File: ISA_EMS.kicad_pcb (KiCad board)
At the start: 2 copper layers, 176.5 x 102.9 mm, 91 parts, among them J1 ISA BUS, J10 Parallel Port, J11 Serial 4 IDC, J12 Serial 3 IDC, J13 UART4_SEL, J14 ROM Config, J2 ADDR_IRQ, J3 UART1_SEL, J4 UART2_SEL, J5 ADDR, J6 Serial 2 IDC, J7 Serial 1 DB9, J8 UART3_SEL, J9 Parport IRQ Select, U1 74LS138, U11 74LS30, U12 74LS86, U13 74LS02, U14 74LS155, U15 74LS245, U16 74LS174, U17 74LS374, U18 74LS05, U19 74LS125, U2 74LS138, U20 74LS240, U21 74LS244, U23 16C554, U24 74LS32, U25 GD75232N, U26 GD75232N, U27 SST39SF040, U28 74HCT688, U5 GD75232N, U6 GD75232N, X1 1.8432Mhz

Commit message: Update schematic, draw board
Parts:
- removed C27, C28, C29, C30, C31, C32, C33, C34, C35: 2.2nF, Capacitor_THT:C_Disc_D5.0mm_W2.5mm_P5.00mm
- removed D2: LED Channel B, LED_THT:LED_D3.0mm-3
- removed D3: LED Channel C, LED_THT:LED_D3.0mm-3
- removed D4: LED Channel D, LED_THT:LED_D3.0mm-3
- removed J10: Parallel Port, Connector_PinHeader_2.54mm:PinHeader_2x13_P2.54mm_Vertical
- removed J11: Serial 4 IDC, Connector_PinHeader_2.54mm:PinHeader_2x05_P2.54mm_Vertical
- removed J12: Serial 3 IDC, Connector_PinHeader_2.54mm:PinHeader_2x05_P2.54mm_Vertical
- removed J13: UART4_SEL, Connector_PinHeader_2.54mm:PinHeader_1x04_P2.54mm_Vertical
- removed the J3 at (227.4, 159.1)
- removed J4: UART2_SEL, Connector_PinHeader_2.54mm:PinHeader_1x08_P2.54mm_Vertical
- removed J5: ADDR, Connector_PinHeader_2.54mm:PinHeader_1x04_P2.54mm_Vertical
- removed J6: Serial 2 IDC, Connector_PinHeader_2.54mm:PinHeader_2x05_P2.54mm_Vertical
- removed J7: Serial 1 DB9, Connector_Dsub:DSUB-9_Male_Horizontal_P2.77x2.84mm_EdgePinOffset7.70mm_Housed_MountingHolesOffset9.12mm
- removed J8: UART3_SEL, Connector_PinHeader_2.54mm:PinHeader_1x04_P2.54mm_Vertical
- removed J9: Parport IRQ Select, Connector_PinHeader_2.54mm:PinHeader_2x04_P2.54mm_Vertical
- removed JP1: Address selection, Connector_PinHeader_2.54mm:PinHeader_1x02_P2.54mm_Vertical
- removed JP2: Parport type, Connector_PinHeader_2.54mm:PinHeader_1x03_P2.54mm_Vertical
- removed JP3: Interrupt Mode, Connector_PinHeader_2.54mm:PinHeader_1x02_P2.54mm_Vertical
- removed R10, R4, R5, R6, R7, R8, R9: 1k, Resistor_THT:R_Axial_DIN0207_L6.3mm_D2.5mm_P10.16mm_Horizontal
- removed the RN1 at (144.8, 124.5)
- removed the U1 at (271.8, 190.5)
- removed the U2 at (271.8, 179.1)
- removed U23: 16C554, Package_LCC:PLCC-68_THT-Socket
- removed U24: 74LS32, Package_DIP:DIP-14_W7.62mm_LongPads
- removed U25, U26: GD75232N, Package_DIP:DIP-20_W7.62mm_LongPads
- removed X1: 1.8432Mhz, ISA_DualUART:Oscillator_DIP-14-8
- added C21: 100nF, Capacitor_THT:C_Disc_D6.0mm_W2.5mm_P5.00mm, F.Cu at (254.0, 104.1)
- added RN3: 10k, Resistor_THT:R_Array_SIP9, F.Cu at (224.8, 177.8)
- added U10: 74HCT32, Package_DIP:DIP-14_W7.62mm_LongPads, F.Cu at (223.5, 156.2)
- added U3: AS6C4008-55PCN, Package_DIP:DIP-32_W15.24mm, F.Cu at (162.6, 108.0)
- added U4: AS6C4008-55PCN, Package_DIP:DIP-32_W15.24mm, F.Cu at (142.2, 108.0)
- added U7: 74HCT688, Package_DIP:DIP-20_W7.62mm_LongPads, F.Cu at (177.8, 190.5)
- added U8: 74HCT688, Package_DIP:DIP-20_W7.62mm_LongPads, F.Cu at (146.1, 190.5)
- added U9: 74HCT139, Package_DIP:DIP-16_W7.62mm_LongPads, F.Cu at (208.3, 153.7)
- D1: value LED Channel A -> EMS in use; footprint LED_THT:LED_D3.0mm-3 -> LED_THT:LED_D3.0mm_Clear
- J2: value ADDR_IRQ -> EMS Address; footprint Connector_PinHeader_2.54mm:PinHeader_1x08_P2.54mm_Vertical -> Connector_PinHeader_2.54mm:PinHeader_2x04_P2.54mm_Vertical
- RN2: value 4.7k -> 10k
- U11: value 74LS30 -> 74HCT04
- U12: value 74LS86 -> 74ACT245; footprint Package_DIP:DIP-14_W7.62mm_LongPads -> Package_DIP:DIP-20_W7.62mm_LongPads
- U13: value 74LS02 -> AS6C4008-55PCN; footprint Package_DIP:DIP-14_W7.62mm_LongPads -> Package_DIP:DIP-32_W15.24mm
- U14: value 74LS155 -> AS6C4008-55PCN; footprint Package_DIP:DIP-16_W7.62mm_LongPads -> Package_DIP:DIP-32_W15.24mm
- U15: value 74LS245 -> AS6C4008-55PCN; footprint Package_DIP:DIP-20_W7.62mm_LongPads -> Package_DIP:DIP-32_W15.24mm
- U16: value 74LS174 -> AS6C4008-55PCN; footprint Package_DIP:DIP-16_W7.62mm_LongPads -> Package_DIP:DIP-32_W15.24mm
- U17: value 74LS374 -> 74HCT138; footprint Package_DIP:DIP-20_W7.62mm_LongPads -> Package_DIP:DIP-16_W7.62mm_LongPads
- U18: value 74LS05 -> 74LS573; footprint Package_DIP:DIP-14_W7.62mm_LongPads -> Package_DIP:DIP-20_W7.62mm_LongPads
- U19: value 74LS125 -> 74LS573; footprint Package_DIP:DIP-14_W7.62mm_LongPads -> Package_DIP:DIP-20_W7.62mm_LongPads
- U20: value 74LS240 -> 74LS573
- U21: value 74LS244 -> 74LS573
- U5, U6: value GD75232N -> AS6C4008-55PCN; footprint Package_DIP:DIP-20_W7.62mm_LongPads -> Package_DIP:DIP-32_W15.24mm
- moved C17 155.1 mm to (142.2, 184.2)
- moved C38 153.6 mm to (294.6, 104.1), turned to 180 degrees
- moved U5 127.9 mm to (182.9, 108.0), turned to 0 degrees
- moved U16 127.8 mm to (284.5, 108.0), turned to 0 degrees
- moved D1 114.3 mm to (304.8, 105.4), turned to 90 degrees
- moved R3 113.0 mm to (304.8, 121.9), turned to 90 degrees
- moved U6 104.9 mm to (203.2, 108.0), turned to 0 degrees
- moved C11 96.7 mm to (174.0, 184.2)
- moved C40 87.7 mm to (152.4, 104.1), turned to 180 degrees
- moved RN1 85.3 mm to (285.8, 157.5)
- moved J3 85.3 mm to (283.2, 163.8)
- moved C36 85.1 mm to (213.4, 104.1), turned to 180 degrees
- moved U14 82.6 mm to (243.8, 108.0), turned to 0 degrees
- moved U13 82.5 mm to (223.5, 108.0), turned to 0 degrees
- moved C2 74.5 mm to (224.8, 152.4), turned to 0 degrees
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- renumbered J14 to J3, RN3 to RN1, U28 to U1, U27 to U2
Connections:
- J1 pad 14: /~IOR -> (no net)
- J1 pad 2: /RESETDRV -> (no net)
- J1 pad 21: /IRQ7 -> (no net)
- J1 pad 23: /IRQ5 -> (no net)
- J1 pad 24: /IRQ4 -> (no net)
- J1 pad 25: /IRQ3 -> (no net)
- J2 pad 1: /IRQ3 -> GND
- J2 pad 2: /IRQ4 -> /JP1
- J2 pad 3: /IRQ5 -> GND
- J2 pad 4: /IRQ7 -> /JP2
- J2 pad 5: /0x2E8 -> GND
- J2 pad 6: /0x3E8 -> /JP3
- J2 pad 7: /0x2F8 -> GND
- J2 pad 8: /0x3F8 -> /JP4
- R3 pad 1: Net-(D1-Pad1) -> /~RAM-SELECT
- R3 pad 2: /TX_A -> Net-(D1-Pad1)
- RN2 pad 2: /~UART1_CS -> /JP1
- RN2 pad 3: /~UART2_CS -> /JP2
- RN2 pad 4: /~UART3_CS -> /JP3
- RN2 pad 5: /~UART4_CS -> /JP4
- U11 pad 11: /A9 -> GND
- U11 pad 12: /A9 -> (no net)
- U11 pad 13: (no net) -> GND
- U11 pad 2: Net-(U11-Pad2) -> /REG0-LOAD
- U11 pad 3: /A3 -> Net-(U11-Pad3)
- U11 pad 4: /A4 -> /REG1-LOAD
- U11 pad 5: /A5 -> Net-(U11-Pad5)
- U11 pad 6: /A6 -> /REG2-LOAD
- U11 pad 8: Net-(U11-Pad8) -> /REG3-LOAD
- U11 pad 9: (no net) -> Net-(U11-Pad9)
- U12 pad 1: /PARPORT_PE -> /~MEMR
- U12 pad 10: VCC -> GND
- U12 pad 11: /PARPORT_IRQ -> /DB7
- U12 pad 12: VCC -> /DB6
- U12 pad 13: /RN_7 -> /DB5
- U12 pad 14: VCC -> /DB4
- U12 pad 2: VCC -> /D0
- U12 pad 3: Net-(U12-Pad3) -> /D1
- U12 pad 4: /RN_1 -> /D2
- U12 pad 5: /A8 -> /D3
- U12 pad 6: Net-(U11-Pad2) -> /D4
- U12 pad 7: GND -> /D5
- U12 pad 8: /~PARPORT_IRQEN -> /D6
- U12 pad 9: /PARPORT_IRQEN -> /D7
- U13 pad 1: Net-(U13-Pad1) -> /RAM-A18
- U13 pad 10: /PARPORT_R -> /A2
- U13 pad 11: /RESETDRV -> /A1
- U13 pad 12: /RESETDRV -> /A0
- U13 pad 13: /~PARPORT_RESET -> /DB0
- U13 pad 14: VCC -> /DB1
- U13 pad 2: /PARPORT_SLCT -> /RAM-A16
- U13 pad 3: /PARPORT_SLCT -> /RAM-A14
- U13 pad 4: Net-(U11-Pad1) -> /A12
- U13 pad 6: /AEN -> /A6
- U13 pad 7: GND -> /A5
- U13 pad 8: Net-(U11-Pad8) -> /A4
- U13 pad 9: /~IOR -> /A3
- U14 pad 1: /PARPORT_R -> /RAM-A18
- U14 pad 10: (no net) -> /A2
- U14 pad 11: /PARPORT_WPC -> /A1
- U14 pad 12: (no net) -> /A0
- U14 pad 13: /A0 -> /DB0
- U14 pad 14: /~IOW -> /DB1
- U14 pad 15: Net-(U11-Pad8) -> /DB2
- U14 pad 16: VCC -> GND
- U14 pad 2: GND -> /RAM-A16
- U14 pad 3: /A1 -> /RAM-A14
- U14 pad 4: (no net) -> /A12
- U14 pad 5: /PARPORT_RPC -> /A7
- U14 pad 6: /PARPORT_RPB -> /A6
- U14 pad 7: /PARPORT_RPA -> /A5
- U14 pad 8: GND -> /A4
- U14 pad 9: /PARPORT_WPA -> /A3
- U15 pad 1: /PARPORT_R -> /RAM-A18
- U15 pad 10: GND -> /A2
- U15 pad 11: /D7 -> /A1
- U15 pad 12: /D6 -> /A0
- U15 pad 13: /D5 -> /DB0
- U15 pad 14: /D4 -> /DB1
- U15 pad 15: /D3 -> /DB2
- U15 pad 16: /D2 -> GND
- U15 pad 17: /D1 -> /DB3
- U15 pad 18: /D0 -> /DB4
- U15 pad 19: GND -> /DB5
- U15 pad 2: /PARPORT_BD0 -> /RAM-A16
- U15 pad 20: VCC -> /DB6
- U15 pad 3: /PARPORT_BD1 -> /RAM-A14
- U15 pad 4: /PARPORT_BD2 -> /A12
- U15 pad 5: /PARPORT_BD3 -> /A7
- U15 pad 6: /PARPORT_BD4 -> /A6
- U15 pad 7: /PARPORT_BD5 -> /A5
- U15 pad 8: /PARPORT_BD6 -> /A4
- U15 pad 9: /PARPORT_BD7 -> /A3
- U16 pad 1: /~PARPORT_RESET -> /RAM-A18
- U16 pad 10: Net-(U16-Pad10) -> /A2
- U16 pad 11: /PARPORT_BD3 -> /A1
- U16 pad 12: /PARPORT_IRQEN -> /A0
- U16 pad 13: /PARPORT_BD4 -> /DB0
- U16 pad 14: /PARPORT_BD5 -> /DB1
- U16 pad 15: /PARPORT_DIR -> /DB2
- U16 pad 16: VCC -> GND
- U16 pad 2: Net-(U16-Pad2) -> /RAM-A16
- U16 pad 3: /PARPORT_BD0 -> /RAM-A14
- U16 pad 4: /PARPORT_BD1 -> /A12
- U16 pad 5: Net-(U16-Pad5) -> /A7
- U16 pad 6: /PARPORT_BD2 -> /A6
- U16 pad 7: Net-(U16-Pad7) -> /A5
- U16 pad 8: GND -> /A4
- U16 pad 9: /PARPORT_WPC -> /A3
- U17 pad 1: Net-(JP2-Pad2) -> /RAM-A19
- U17 pad 10: GND -> /~RAM-CS5
- U17 pad 11: /PARPORT_WPA -> /~RAM-CS4
- U17 pad 12: /PARPORT_DATA3 -> /~RAM-CS3
- U17 pad 13: /PARPORT_BD3 -> /~RAM-CS2
- U17 pad 14: /PARPORT_BD2 -> /~RAM-CS1
- U17 pad 15: /PARPORT_DATA2 -> /~RAM-CS0
- U17 pad 16: /PARPORT_DATA1 -> VCC
- U17 pad 2: /PARPORT_DATA4 -> /RAM-A20
- U17 pad 3: /PARPORT_BD4 -> /RAM-A21
- U17 pad 4: /PARPORT_BD5 -> GND
- U17 pad 5: /PARPORT_DATA5 -> /~RAM-SELECT
- U17 pad 6: /PARPORT_DATA6 -> VCC
- U17 pad 7: /PARPORT_BD6 -> /~RAM-CS7
- U17 pad 8: /PARPORT_BD7 -> GND
- U17 pad 9: /PARPORT_DATA7 -> /~RAM-CS6
- U18 pad 1: Net-(U16-Pad2) -> /~REG0-OE
- U18 pad 10: /RN_4 -> GND
- U18 pad 11: /RN_3 -> /REG0-LOAD
- U18 pad 12: /RN_8 -> /RAM-A21
- U18 pad 13: /RN_4 -> /RAM-A20
- U18 pad 14: VCC -> /RAM-A19
- U18 pad 2: /RN_6 -> /D0
- U18 pad 3: Net-(U16-Pad7) -> /D1
- U18 pad 4: /RN_3 -> /D2
- U18 pad 5: Net-(U16-Pad5) -> /D3
- U18 pad 6: /RN_5 -> /D4
- U18 pad 7: GND -> /D5
- U18 pad 8: /RN_2 -> /D6
- U18 pad 9: Net-(U16-Pad10) -> /D7
- U19 pad 1: VCC -> /~REG1-OE
- U19 pad 10: /PARPORT_RPC -> GND
- U19 pad 11: Net-(J9-Pad2) -> /REG1-LOAD
- U19 pad 12: /RN_7 -> /RAM-A21
- U19 pad 13: /~PARPORT_IRQEN -> /RAM-A20
- U19 pad 14: VCC -> /RAM-A19
- U19 pad 2: VCC -> /D0
- U19 pad 3: (no net) -> /D1
- U19 pad 4: /PARPORT_RPB -> /D2
- U19 pad 5: /~PARPORT_ERROR -> /D3
- U19 pad 6: /PARPORT_BD3 -> /D4
- U19 pad 7: GND -> /D5
- U19 pad 8: /PARPORT_BD4 -> /D6
- U19 pad 9: /PARPORT_IRQEN -> /D7
- U20 pad 1: /PARPORT_RPB -> /~REG2-OE
- U20 pad 11: /RN_2 -> /REG2-LOAD
- U20 pad 12: /PARPORT_BD7 -> /RAM-A21
- U20 pad 13: /RN_8 -> /RAM-A20
- U20 pad 14: /PARPORT_BD6 -> /RAM-A19
- U20 pad 15: /RN_5 -> /RAM-A18
- U20 pad 16: /PARPORT_BD5 -> /RAM-A17
- U20 pad 17: /RN_6 -> /RAM-A16
- U20 pad 18: /PARPORT_BD4 -> /RAM-A15
- U20 pad 19: /PARPORT_RPC -> /RAM-A14
- U20 pad 2: Net-(U13-Pad1) -> /D0
- U20 pad 3: /PARPORT_BD0 -> /D1
- U20 pad 4: Net-(U12-Pad3) -> /D2
- U20 pad 5: /PARPORT_BD1 -> /D3
- U20 pad 6: /PARPORT_IRQ -> /D4
- U20 pad 7: /PARPORT_BD2 -> /D5
- U20 pad 8: /PARPORT_BUSY -> /D6
- U20 pad 9: /PARPORT_BD3 -> /D7
- U21 pad 1: /PARPORT_RPA -> /~REG3-OE
- U21 pad 11: /PARPORT_DATA3 -> /REG3-LOAD
- U21 pad 12: /PARPORT_BD7 -> /RAM-A21
- U21 pad 13: /PARPORT_DATA2 -> /RAM-A20
- U21 pad 14: /PARPORT_BD6 -> /RAM-A19
- U21 pad 15: /PARPORT_DATA1 -> /RAM-A18
- U21 pad 16: /PARPORT_BD5 -> /RAM-A17
- U21 pad 17: /PARPORT_DATA0 -> /RAM-A16
- U21 pad 18: /PARPORT_BD4 -> /RAM-A15
- U21 pad 19: /PARPORT_RPA -> /RAM-A14
- U21 pad 2: /PARPORT_DATA4 -> /D0
- U21 pad 3: /PARPORT_BD0 -> /D1
- U21 pad 4: /PARPORT_DATA5 -> /D2
- U21 pad 5: /PARPORT_BD1 -> /D3
- U21 pad 6: /PARPORT_DATA6 -> /D4
- U21 pad 7: /PARPORT_BD2 -> /D5
- U21 pad 8: /PARPORT_DATA7 -> /D6
- U21 pad 9: /PARPORT_BD3 -> /D7
- U5 pad 1: +12V -> /RAM-A18
- U5 pad 10: -12V -> /A2
- U5 pad 11: GND -> /A1
- U5 pad 12: /~RI_A -> /A0
- U5 pad 13: /~DTR_A -> /DB0
- U5 pad 14: /~CTS_A -> /DB1
- U5 pad 15: /TX_A -> /DB2
- U5 pad 16: /~RTS_A -> GND
- U5 pad 17: /RX_A -> /DB3
- U5 pad 18: /~DSR_A -> /DB4
- U5 pad 19: /~DCD_A -> /DB5
- U5 pad 2: /RS232_1_DCD -> /RAM-A16
- U5 pad 20: VCC -> /DB6
- U5 pad 3: /RS232_1_DSR -> /RAM-A14
- U5 pad 4: /RS232_1_RX -> /A12
- U5 pad 5: /RS232_1_RTS -> /A7
- U5 pad 6: /RS232_1_TX -> /A6
- U5 pad 7: /RS232_1_CTS -> /A5
- U5 pad 8: /RS232_1_DTR -> /A4
- U5 pad 9: /RS232_1_RI -> /A3
- U6 pad 1: +12V -> /RAM-A18
- U6 pad 10: -12V -> /A2
- U6 pad 11: GND -> /A1
- U6 pad 12: /~RI_B -> /A0
- U6 pad 13: /~DTR_B -> /DB0
- U6 pad 14: /~CTS_B -> /DB1
- U6 pad 15: /TX_B -> /DB2
- U6 pad 16: /~RTS_B -> GND
- U6 pad 17: /RX_B -> /DB3
- U6 pad 18: /~DSR_B -> /DB4
- U6 pad 19: /~DCD_B -> /DB5
- U6 pad 2: /RS232_2_DCD -> /RAM-A16
- U6 pad 20: VCC -> /DB6
- U6 pad 3: /RS232_2_DSR -> /RAM-A14
- U6 pad 4: /RS232_2_RX -> /A12
- U6 pad 5: /RS232_2_RTS -> /A7
- U6 pad 6: /RS232_2_TX -> /A6
- U6 pad 7: /RS232_2_CTS -> /A5
- U6 pad 8: /RS232_2_DTR -> /A4
- U6 pad 9: /RS232_2_RI -> /A3
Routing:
- net GND: track 995.6 -> 0.00 mm, vias 1 -> 0
- net VCC: track 784.3 -> 0.00 mm, vias 1 -> 0
- net /~IOW: track 221.8 -> 0.00 mm, vias 5 -> 0
- net /A5: track 215.0 -> 0.00 mm, vias 3 -> 0
- net /A3: track 214.5 -> 0.00 mm, vias 3 -> 0
- net +12V: track 212.6 -> 0.00 mm, vias 2 -> 0
- net /A4: track 211.9 -> 0.00 mm, vias 4 -> 0
- net /RESETDRV: track 209.8 -> 0.00 mm, vias 2 -> 0
- net /A6: track 206.4 -> 0.00 mm, vias 2 -> 0
- net /D6: track 204.3 -> 0.00 mm, vias 4 -> 0
- net -12V: track 195.6 -> 0.00 mm, vias 1 -> 0
- net /A1: track 190.6 -> 0.00 mm, vias 5 -> 0
- net /D7: track 189.2 -> 0.00 mm, vias 1 -> 0
- net /A0: track 176.4 -> 0.00 mm, vias 4 -> 0
- net /PARPORT_IRQ: track 175.4 -> 0.00 mm, vias 1 -> 0
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- removed copper zone on B.Cu, net GND
- removed copper zone on F.Cu, net GND
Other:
- board text removed: "1-2 -> Bidirectional 2-3 -> SPP (default)"
- board text removed: "1.8432Mhz"
- board text removed: "10k"
- board text removed: "10k Bussed"
- board text removed: "10uF"
- board text removed: "16C554"
- board text removed: "1k"
- board text removed: "2E8"
- board text removed: "2F8"
- board text removed: "32K"
- board text removed: "3E8"
- board text removed: "3F8"
- board text removed: "4.7k Bussed"
- board text removed: "4.7k bussed"
- board text removed: "64K"
- board text removed: "74HCT688"
- board text removed: "74LS02"
- board text removed: "74LS05"
- board text removed: "74LS125"
- board text removed: "74LS138"
- board text removed: "74LS155"
- board text removed: "74LS174"
- board text removed: "74LS240"
- board text removed: "74LS244"
- board text removed: "74LS245"
- board text removed: "74LS30"
- board text removed: "74LS32"
- board text removed: "74LS374"
- board text removed: "74LS86"
- board text removed: "75232"
- board text removed: "<- 9x 2.2nF ->"
- board text removed: "A15"
- board text removed: "A16"
- board text removed: "A17"
- board text removed: "A18"
- board text removed: "Ch.1"
- board text removed: "Ch.2"
- board text removed: "Ch.3"
- board text removed: "Ch.4"
- board text removed: "ENA"
- board text removed: "INT Mode"
- board text removed: "IRQ3"
- board text removed: "IRQ4"
- board text removed: "IRQ5"
- board text removed: "IRQ7"
- board text removed: "Open -> 0x278 Closed -> 0x378"
- board text removed: "ParPort IRQ"
- board text removed: "Parallel Port"
- board text removed: "ROM EXP"
- board text removed: "SER1"
- board text removed: "SER2"
- board text removed: "SER3"
- board text removed: "SER4"
- board text removed: "SST39SF0x0"
- board text removed: "Serial / Parallel / ROM ISA Board - 1.0 by hkz"
- board text removed: "Serial port 1"
- board text removed: "Serial port 2"
- board text removed: "Serial port 3"
- board text removed: "Serial port 4"

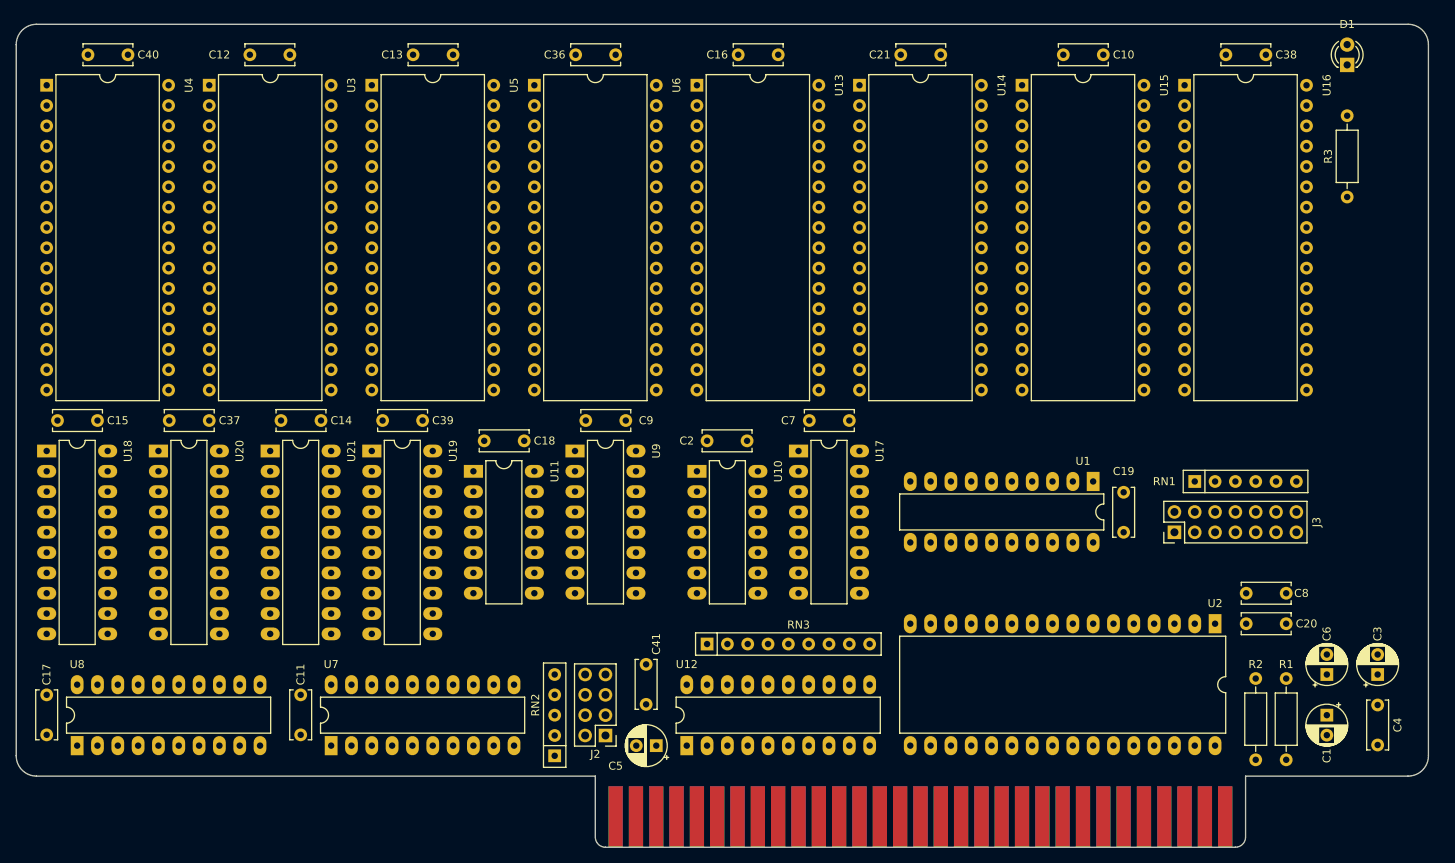
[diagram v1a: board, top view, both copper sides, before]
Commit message: Routed the board
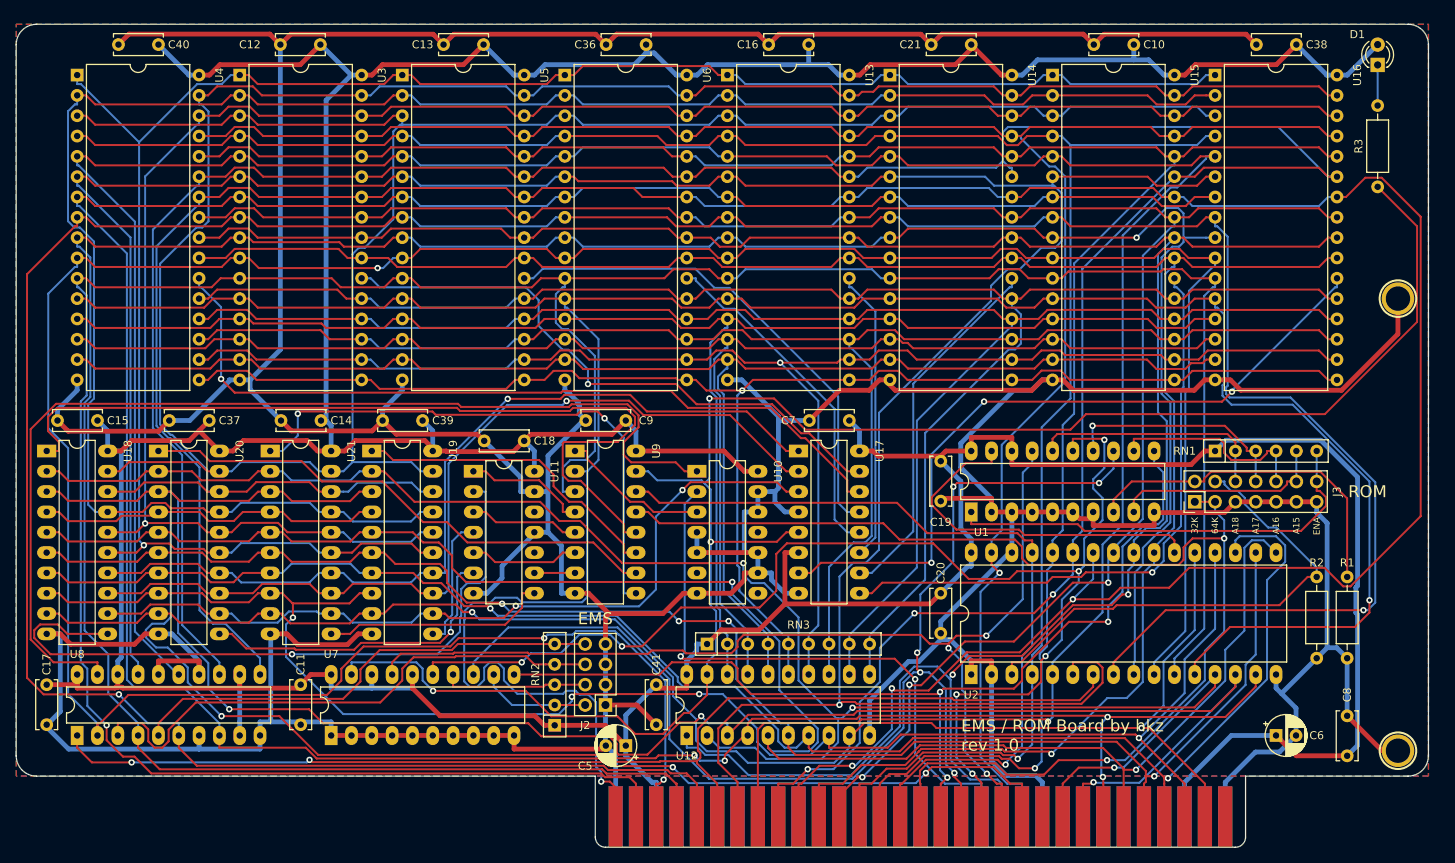
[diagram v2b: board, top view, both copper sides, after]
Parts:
- removed C1, C3: 10uF, Capacitor_THT:CP_Radial_D5.0mm_P2.50mm
- removed C2, C4: 100nF, Capacitor_THT:C_Disc_D6.0mm_W2.5mm_P5.00mm
- added H1: MountingHole_Pad, skiselev_footprints:Hole_3mm, F.Cu at (311.1, 191.1)
- added H2: MountingHole_Pad, skiselev_footprints:Hole_3mm, F.Cu at (311.1, 134.6)
- moved C20 43.3 mm to (254.0, 171.4), turned to 270 degrees
- moved U2 31.1 mm to (257.8, 181.6), turned to 90 degrees
- moved C19 24.5 mm to (254.0, 154.9), turned to 270 degrees
- moved C8 21.7 mm to (304.8, 191.8), turned to 90 degrees
- moved U1 15.7 mm to (257.8, 161.3), turned to 90 degrees
- moved R1 14.8 mm to (304.8, 179.6)
- moved R2 14.8 mm to (301.0, 179.6)
- moved C6 9.92 mm to (295.9, 189.2), turned to 0 degrees
- moved J3 4.58 mm to (285.8, 160.0)
- moved RN1 4.58 mm to (288.3, 153.7)
- moved C10 4.02 mm to (278.1, 102.9)
- moved C12 4.02 mm to (171.4, 102.9)
- moved C13 4.02 mm to (196.8, 102.9)
- moved C16 4.02 mm to (237.5, 102.9)
- moved C21 4.02 mm to (257.8, 102.9)
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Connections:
- J1 pad 7: -12V -> (no net)
- J1 pad 9: +12V -> (no net)
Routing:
- net GND: track 0.00 -> 899.8 mm
- net VCC: track 0.00 -> 690.6 mm
- net /A4: track 0.00 -> 402.8 mm, vias 0 -> 2
- net /A9: track 0.00 -> 375.9 mm, vias 0 -> 3
- net /A1: track 0.00 -> 367.2 mm, vias 0 -> 1
- net /A2: track 0.00 -> 366.6 mm, vias 0 -> 3
- net /A6: track 0.00 -> 364.8 mm, vias 0 -> 1
- net /A8: track 0.00 -> 357.7 mm, vias 0 -> 3
- net /A5: track 0.00 -> 354.9 mm
- net /A3: track 0.00 -> 352.4 mm, vias 0 -> 1
- net /A7: track 0.00 -> 347.2 mm, vias 0 -> 1
- net /A0: track 0.00 -> 334.6 mm, vias 0 -> 2
- net /~MEMR: track 0.00 -> 291.9 mm, vias 0 -> 2
- net /A13: track 0.00 -> 258.4 mm, vias 0 -> 1
- net /A10: track 0.00 -> 255.1 mm, vias 0 -> 1
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- added copper zone on B.Cu, net GND
- added copper zone on F.Cu, net GND
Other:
- board text added: "32K"
- board text added: "64K"
- board text added: "A15"
- board text added: "A16"
- board text added: "A17"
- board text added: "A18"
- board text added: "EMS"
- board text added: "EMS / ROM Board by hkz rev 1.0"
- board text added: "ENA"
- board text added: "ROM"

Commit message: Update the silkscreen
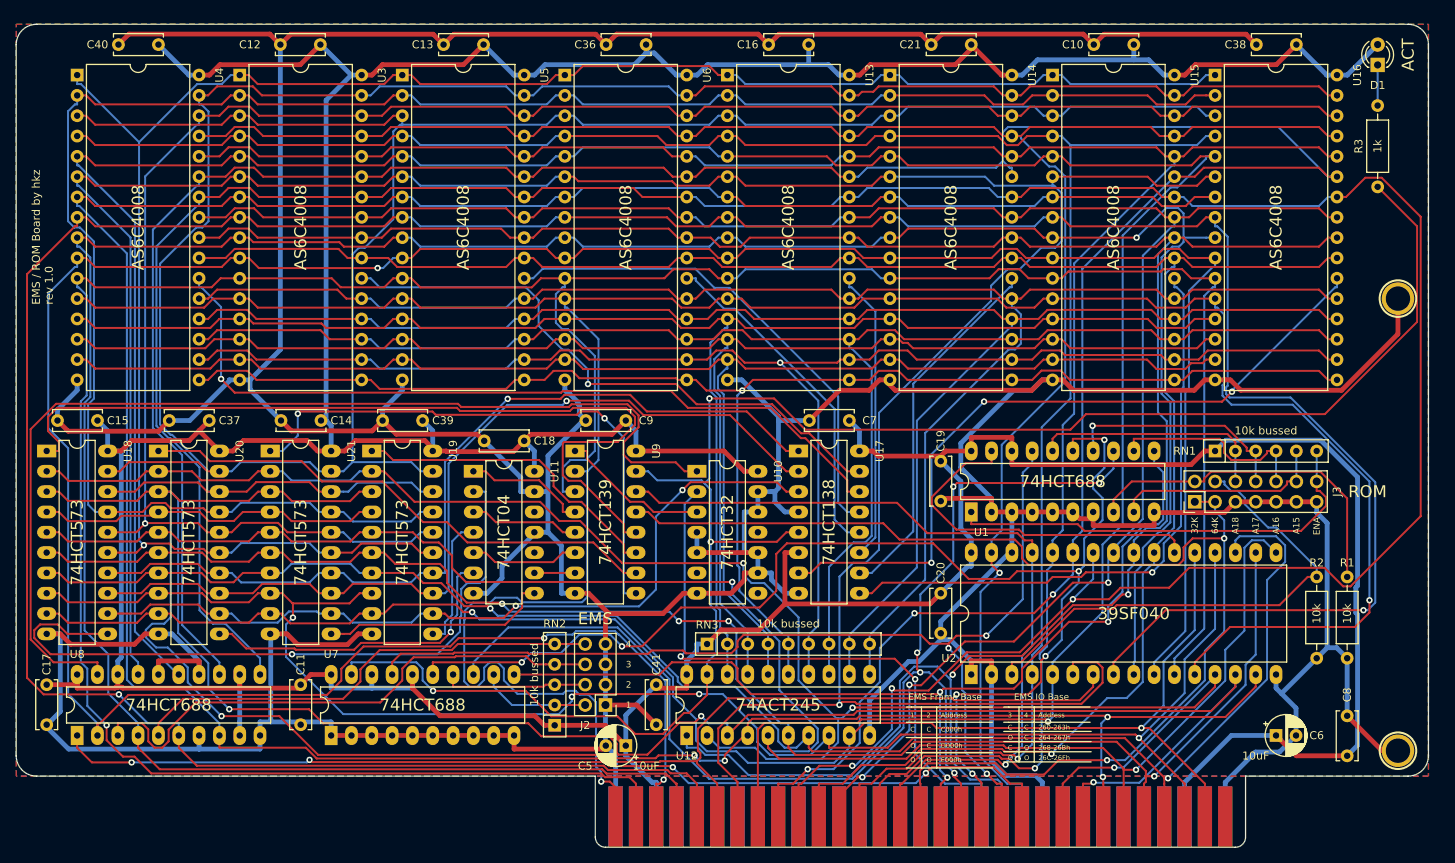
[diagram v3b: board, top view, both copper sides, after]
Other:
- board text added: "1"
- board text added: "10k"
- board text added: "10k bussed"
- board text added: "10uF"
- board text added: "1k"
- board text added: "2"
- board text added: "260-263h"
- board text added: "264-267h"
- board text added: "268-26Bh"
- board text added: "26C-26Fh"
- board text added: "3"
- board text added: "39SF040"
- board text added: "4"
- board text added: "74ACT245"
- board text added: "74HCT04"
- board text added: "74HCT138"
- board text added: "74HCT139"
- board text added: "74HCT32"
- board text added: "74HCT573"
- board text added: "74HCT688"
- board text added: "ACT"
- board text added: "AS6C4008"
- board text added: "Address"
- board text added: "C"
- board text added: "C000h"
- board text added: "D000h"
- board text added: "E000h"
- board text added: "EMS Frame Base"
- board text added: "EMS IO Base"
- board text added: "O"

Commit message: Added missing cap
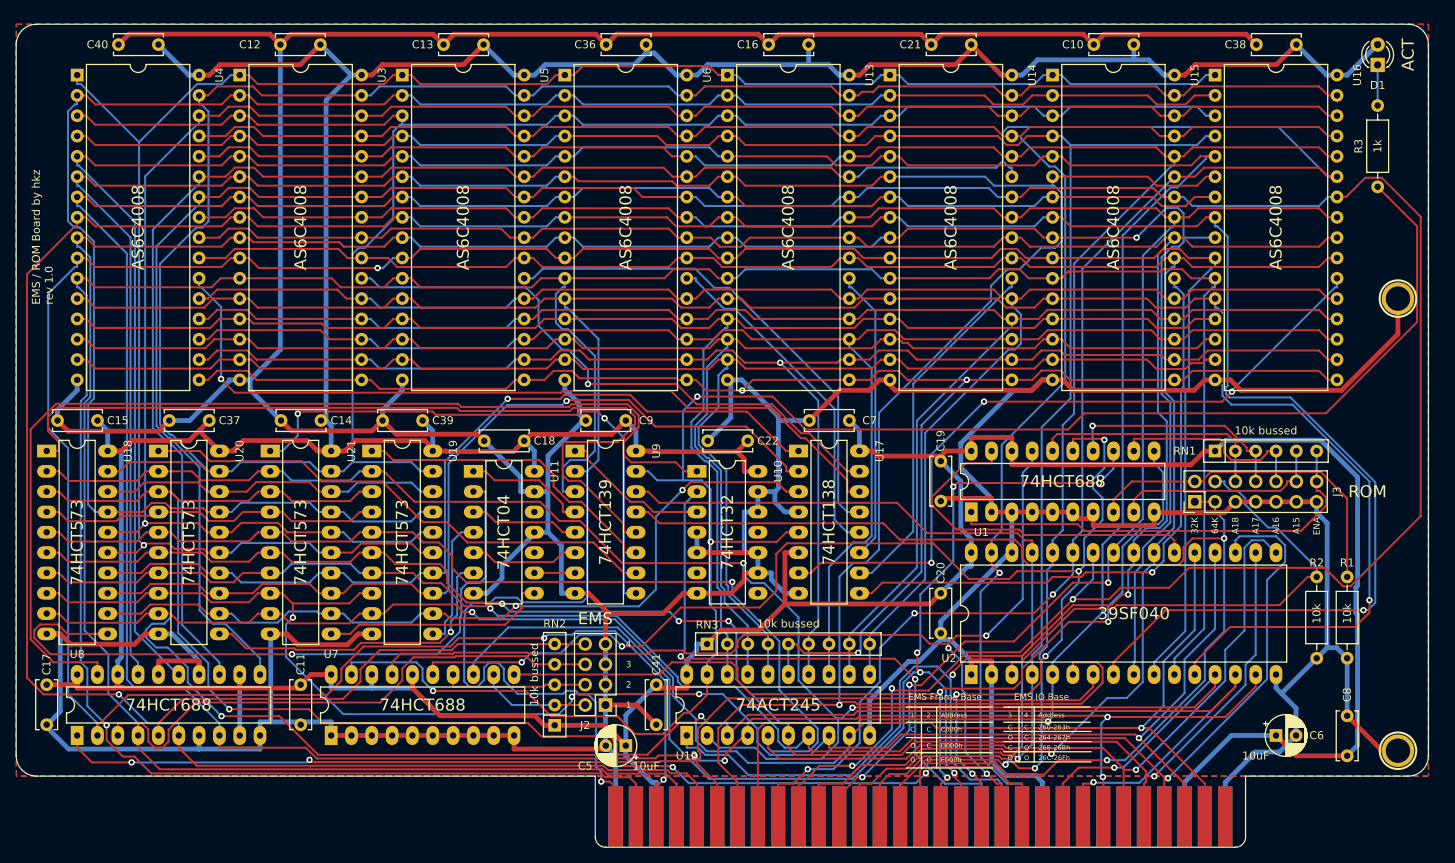
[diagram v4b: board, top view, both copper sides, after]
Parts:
- added C22: 100nF, Capacitor_THT:C_Disc_D6.0mm_W2.5mm_P5.00mm, F.Cu at (229.9, 152.4)
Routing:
- net /DB3: track 187.7 -> 201.9 mm, vias 1 -> 3
- net GND: track 899.8 -> 908.6 mm
- net VCC: track 690.6 -> 693.4 mm
- net /DB2: track 191.4 -> 193.6 mm
- net /DB0: track 195.1 -> 197.2 mm
- net /DB1: track 193.2 -> 195.3 mm
- net /~RAM-SELECT: track 226.2 -> 228.1 mm
